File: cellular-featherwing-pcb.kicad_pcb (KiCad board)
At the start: 2 copper layers, 27 x 54 mm, 80 parts, among them J1 SIM8060-6-0-14-00-A, J2 TSM-116-01-L-SV, J3 TSM-112-01-L-SV, J4 U.FL-R-SMT, J5 U.FL-R-SMT, J5 U.FL-R-SMT(10), U1 BG96, U2 TPS63020QDSJTQ1, U3 TXB0108DQSR, U4 MAX8868EUK30+T

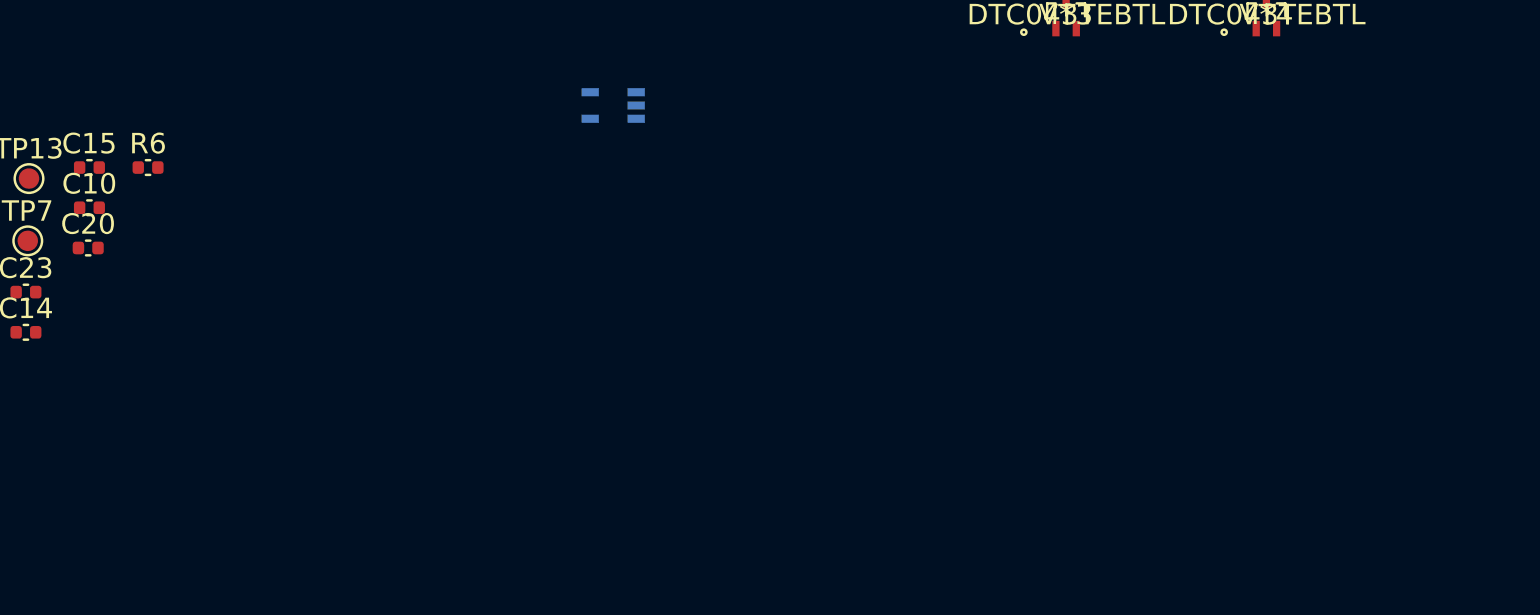
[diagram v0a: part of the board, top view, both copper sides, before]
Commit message: Fixed drc and imported to pcb
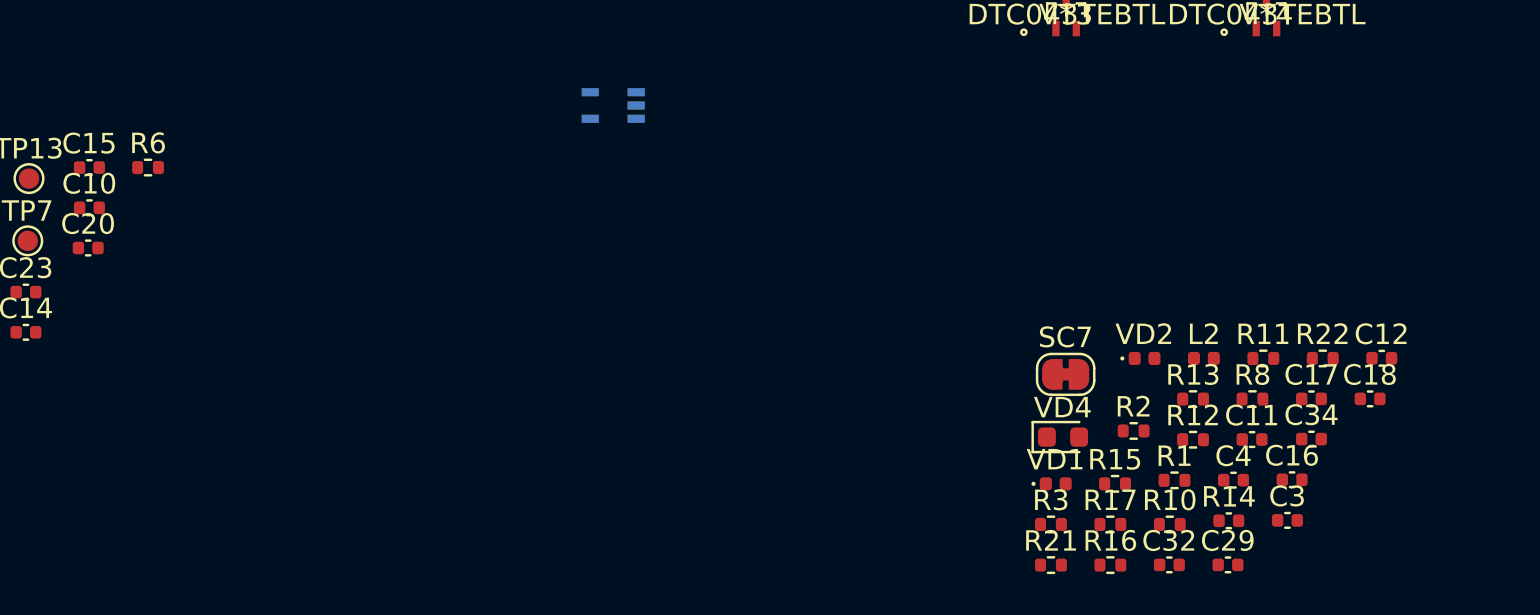
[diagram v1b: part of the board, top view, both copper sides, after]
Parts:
- added C11: 0.1, Capacitor_SMD:C_0402_1005Metric, F.Cu at (155.8, 153.5)
- added C12: 100pF, Capacitor_SMD:C_0402_1005Metric, F.Cu at (162.1, 149.5)
- added C16: 33pF, Capacitor_SMD:C_0402_1005Metric, F.Cu at (157.7, 155.5)
- added C17: 33pF, Capacitor_SMD:C_0402_1005Metric, F.Cu at (158.7, 151.5)
- added C18: 33pF, Capacitor_SMD:C_0402_1005Metric, F.Cu at (161.5, 151.5)
- added C29: 0.1, Capacitor_SMD:C_0402_1005Metric, F.Cu at (154.6, 159.7)
- added C3: 2.2uF, Capacitor_SMD:C_0402_1005Metric, F.Cu at (157.5, 157.5)
- added C32: 0.1, Capacitor_SMD:C_0402_1005Metric, F.Cu at (151.7, 159.7)
- added C34: 0.1, Capacitor_SMD:C_0402_1005Metric, F.Cu at (158.7, 153.5)
- added C4: 0.1uF, Capacitor_SMD:C_0402_1005Metric, F.Cu at (154.8, 155.5)
- added L2: 47nH, Inductor_SMD:L_0402_1005Metric, F.Cu at (153.4, 149.6)
- added R1: 1.24M, Resistor_SMD:R_0402_1005Metric, F.Cu at (151.9, 155.5)
- added R10: 10k, Resistor_SMD:R_0402_1005Metric, F.Cu at (151.7, 157.7)
- added R11: 1k, Resistor_SMD:R_0402_1005Metric, F.Cu at (156.3, 149.6)
- added R12: 1k, Resistor_SMD:R_0402_1005Metric, F.Cu at (152.9, 153.5)
- added R13: 1k, Resistor_SMD:R_0402_1005Metric, F.Cu at (152.9, 151.5)
- added R14: 470, Capacitor_SMD:C_0402_1005Metric, F.Cu at (154.6, 157.5)
- added R15: 100k, Resistor_SMD:R_0402_1005Metric, F.Cu at (149.0, 155.7)
- added R16: 10k, Resistor_SMD:R_0402_1005Metric, F.Cu at (148.8, 159.7)
- added R17: 10k, Resistor_SMD:R_0402_1005Metric, F.Cu at (148.8, 157.7)
- added R2: 182k, Resistor_SMD:R_0402_1005Metric, F.Cu at (149.9, 153.1)
- added R21: 0, Resistor_SMD:R_0402_1005Metric, F.Cu at (145.9, 159.7)
- added R22: 0, Resistor_SMD:R_0402_1005Metric, F.Cu at (159.2, 149.6)
- added R3: 0, Resistor_SMD:R_0402_1005Metric, F.Cu at (145.9, 157.7)
- added R8: 15k, Resistor_SMD:R_0402_1005Metric, F.Cu at (155.8, 151.5)
- added SC7: SolderJumper_2_Bridged, Jumper:SolderJumper-2_P1.3mm_Bridged_RoundedPad1.0x1.5mm, F.Cu at (146.6, 150.3)
- added VD1: D_TVS, Diode_SMD:D_0402_1005Metric, F.Cu at (146.1, 155.7)
- added VD2: D_TVS, Diode_SMD:D_0402_1005Metric, F.Cu at (150.5, 149.6)
- added VD4: BLUE, LED_SMD:LED_0603_1608Metric, F.Cu at (146.5, 153.4)
- R6: footprint Capacitor_SMD:C_0402_1005Metric -> Resistor_SMD:R_0402_1005Metric
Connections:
- D1 pad 1: unconnected-(D1-Pad1) -> Net-(J1-PadC7)

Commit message: starting component layout
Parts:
- moved SC7 165.2 mm to (25.4, 38.1)
- moved C18 118.9 mm to (264.2, 91.4)
- moved C16 118.1 mm to (259.1, 94.8)
- moved C17 117.0 mm to (259.1, 91.4)
- moved SO18 114.3 mm to (17.8, 53.3)
- moved C11 112.9 mm to (261.6, 114.3)
- moved SO13 111.7 mm to (25.1, 33.0)
- moved SO14 105.6 mm to (30.5, 33.0)
- moved SO17 104.8 mm to (25.4, 58.4)
- moved R8 103.6 mm to (251.5, 111.8)
- moved R3 102.8 mm to (233.7, 104.1)
- moved R21 102.2 mm to (236.2, 111.8)
- moved J1 100.1 mm to (246.4, 99.1)
- moved D1 99.6 mm to (259.1, 104.1)
- moved SO15 99.1 mm to (30.5, 38.1)
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
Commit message: Placement work
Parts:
- moved locked 111.0 mm to (146.3, 104.7), turned to 180 degrees
- moved J4 47.4 mm to (218.2, 136.9)
- moved J5 47.4 mm to (213.0, 136.9)
- moved U1 43.7 mm to (163.7, 42.4)
- moved J3 36.9 mm to (151.4, 84.3), turned to 180 degrees
- moved C11 33.2 mm to (252.1, 82.5), turned to -90 degrees
- moved U4 32.5 mm to (97.1, 68.2)
- moved U3 31.1 mm to (199.1, 54.7)
- moved R21 29.6 mm to (253.1, 87.5), turned to 90 degrees
- moved J1 25.5 mm to (248.9, 73.7), turned to 180 degrees
- moved R22 24.1 mm to (249.5, 87.9), turned to 90 degrees
- moved D1 23.5 mm to (248.9, 83.0)
- moved FB1 23.1 mm to (106.7, 93.7)
- moved R3 22.5 mm to (246.6, 85.7), turned to 90 degrees
- moved C18 19.5 mm to (246.6, 83.0), turned to -90 degrees
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- renumbered J2 to locked
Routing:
- net Net-(J1-PadC3): track 0.00 -> 7.22 mm
- net Net-(J1-PadC2): track 0.00 -> 2.84 mm
- net Net-(J1-PadC7): track 0.00 -> 2.12 mm
- net SIM_VDD: track 0.00 -> 1.56 mm
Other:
- board size 27 x 54 mm -> 54 x 27 mm

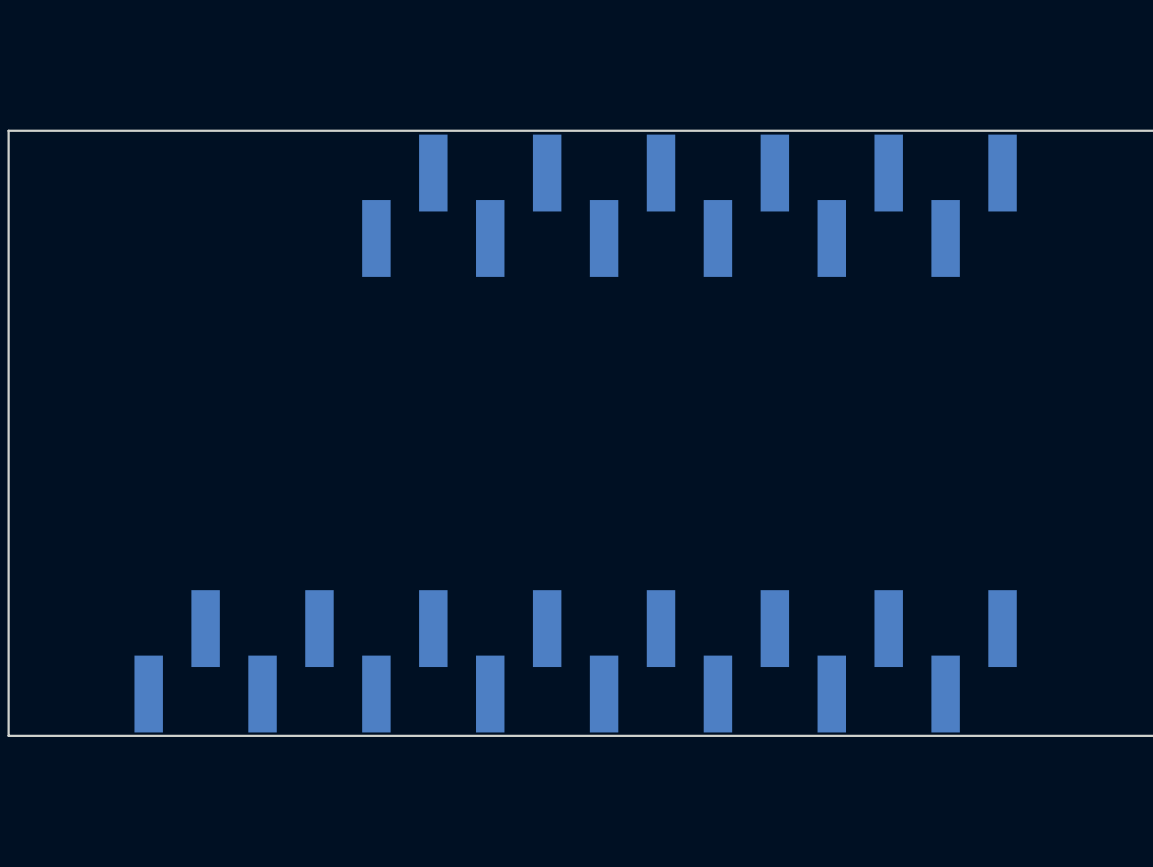
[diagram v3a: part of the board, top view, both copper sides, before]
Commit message: Finished board outline and feather placements
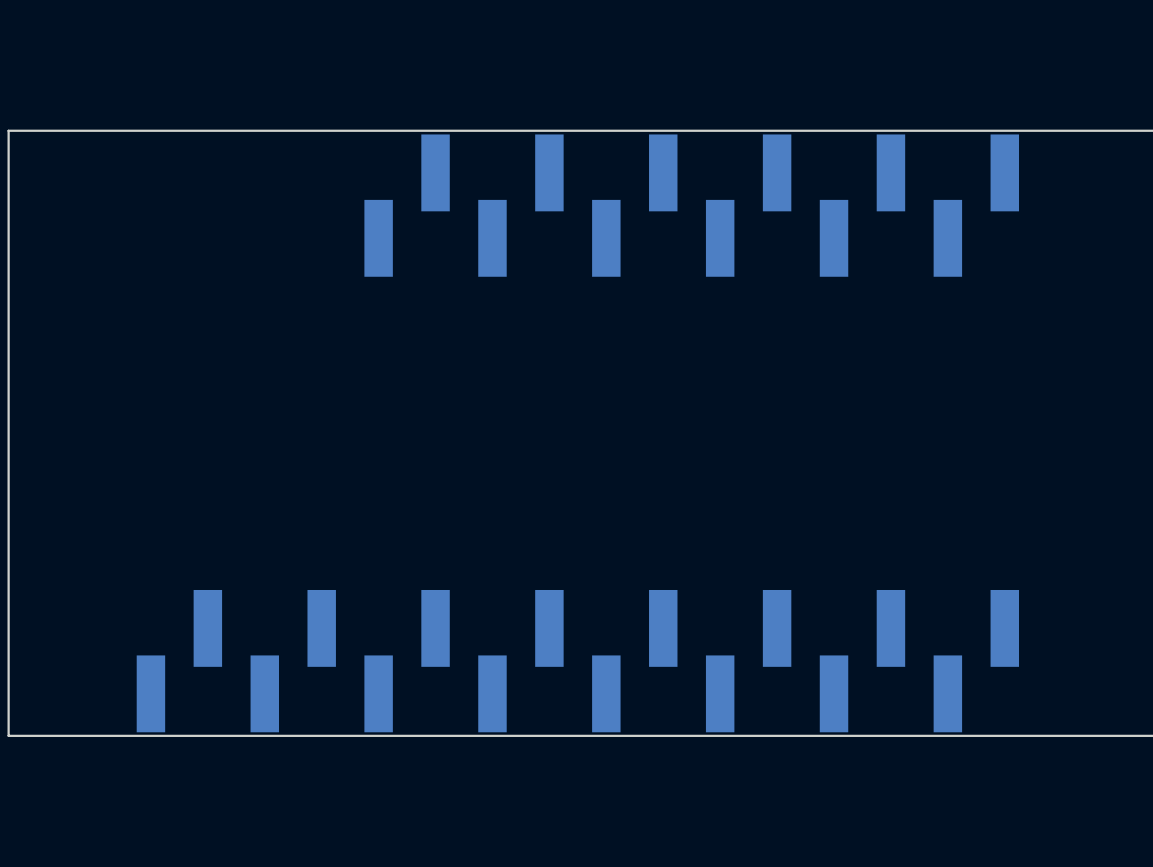
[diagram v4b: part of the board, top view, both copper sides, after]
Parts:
- moved J2 0.10 mm to (146.4, 104.7)
- moved J3 0.10 mm to (151.5, 84.3)
- renumbered locked to J2
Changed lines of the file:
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@@
       (net 24 "GSM_DTR") (pinfunction "1") (pintype "passive"))
   )
-  (footprint "TSM-116-01-L-SV:SAMTEC_TSM-116-01-L-SV" (layer "B.Cu")
-    (at 146.3 104.67375 180)
+  (footprint "TSM-116-01-L-SV:SAMTEC_TSM-116-01-L-SV" locked (layer "B.Cu")
+    (at 146.4 104.666 180)
     (property "MANUFACTURER" "SAMTEC")
     (property "MPN" "TSM-116-01-L-SV")
@@
     (property "Sheetname" "")
     (attr through_hole)
-    (fp_text reference locked "J2" (at -17.145 4.825) (layer "B.SilkS")
+    (fp_text reference "J2" (at 21.4 0) (layer "B.SilkS")
       (effects (font (size 1 1) (thickness 0.15)) (justify mirror))
     )
@@
     (fp_line (start -20.32 -1.27) (end -17.78 -1.27) (layer "B.SilkS") (width 0.2))
     (fp_line (start 17.78 1.27) (end 20.32 1.27) (layer "B.SilkS") (width 0.2))
-    (fp_circle (center 19.3 -3.935) (end 19.4 -3.935) (layer "B.SilkS") (width 0.2) (fill none))
+    (fp_circle (center 20.3 -2.1) (end 20.4 -2.1) (layer "B.SilkS") (width 0.2) (fill none))
     (fp_line (start -20.57 3.425) (end 20.57 3.425) (layer "B.CrtYd") (width 0.05))
     (fp_line (start -20.57 -3.425) (end -20.57 3.425) (layer "B.CrtYd") (width 0.05))
@@
     (fp_line (start 20.32 -1.27) (end -20.32 -1.27) (layer "B.Fab") (width 0.1))
     (fp_line (start -20.32 1.27) (end 20.32 1.27) (layer "B.Fab") (width 0.1))
-    (fp_circle (center 19.3 -3.935) (end 19.4 -3.935) (layer "B.Fab") (width 0.2) (fill none))
+    (fp_circle (center 20.3 -2.1) (end 20.4 -2.1) (layer "B.Fab") (width 0.2) (fill none))
     (pad "01" smd rect locked (at 19.05 -1.46 180) (size 1.27 3.43) (layers "B.Cu" "B.Paste" "B.Mask")
       (net 31 "unconnected-(J2-Pad01)") (pinfunction "01") (pintype "passive"))
@@
     (pad "16" smd rect locked (at -19.05 1.46 180) (size 1.27 3.43) (layers "B.Cu" "B.Paste" "B.Mask")
       (net 39 "unconnected-(J2-Pad16)") (pinfunction "16") (pintype "passive"))
+    (model "${KIPRJMOD}/snapeda/TSM-116-01-L-SV/TSM-116-01-L-SV.step"
+      (offset (xyz 0 0 1.3))
+      (scale (xyz 1 1 1))
+      (rotate (xyz -90 0 0))
+    )
   )
   (footprint "SN74AHC1G09DCKR:SN74AHC1G09DCKR" (layer "B.Cu")
@@
       (net 98 "Net-(U4-Pad5)") (pinfunction "BP") (pintype "output"))
   )
-  (footprint "TSM-112-01-L-SV:SAMTEC_TSM-112-01-L-SV" (layer "B.Cu")
-    (at 151.38 84.34625 180)
+  (footprint "TSM-112-01-L-SV:SAMTEC_TSM-112-01-L-SV" locked (layer "B.Cu")
+    (at 151.48 84.34 180)
     (property "MANUFACTURER" "SAMTEC")
     (property "MPN" "TSM-112-01-L-SV")
@@
     (property "Sheetname" "")
     (attr through_hole)
-    (fp_text reference "J3" (at -12.065 4.825) (layer "B.SilkS")
+    (fp_text reference "J3" (at 16.48 0) (layer "B.SilkS")
       (effects (font (size 1 1) (thickness 0.15)) (justify mirror))
     )
@@
     (fp_line (start 15.24 1.27) (end 15.24 -1.27) (layer "B.SilkS") (width 0.2))
     (fp_line (start 12.7 1.27) (end 15.24 1.27) (layer "B.SilkS") (width 0.2))
-    (fp_circle (center 14.22 -3.935) (end 14.32 -3.935) (layer "B.SilkS") (width 0.2) (fill none))
+    (fp_circle (center 15.2 -2.2) (end 15.3 -2.2) (layer "B.SilkS") (width 0.2) (fill none))
     (fp_line (start 15.49 3.425) (end 15.49 -3.425) (layer "B.CrtYd") (width 0.05))
     (fp_line (start -15.49 3.425) (end 15.49 3.425) (layer "B.CrtYd") (width 0.05))
@@
     (fp_line (start 15.24 1.27) (end 15.24 -1.27) (layer "B.Fab") (width 0.1))
     (fp_line (start -15.24 1.27) (end 15.24 1.27) (layer "B.Fab") (width 0.1))
-    (fp_circle (center 14.22 -3.935) (end 14.32 -3.935) (layer "B.Fab") (width 0.2) (fill none))
+    (fp_circle (center 15.2 -2.2) (end 15.3 -2.2) (layer "B.Fab") (width 0.2) (fill none))
     (pad "01" smd rect locked (at 13.97 -1.46 180) (size 1.27 3.43) (layers "B.Cu" "B.Paste" "B.Mask")
       (net 51 "VBAT") (pinfunction "01") (pintype "passive"))
@@
     (pad "12" smd rect locked (at -13.97 1.46 180) (size 1.27 3.43) (layers "B.Cu" "B.Paste" "B.Mask")
       (net 60 "I2C_SDA") (pinfunction "12") (pintype "passive"))
+    (model "${KIPRJMOD}/snapeda/TSM-112-01-L-SV/TSM-112-01-L-SV.step"
+      (offset (xyz 0 0 1.3))
+      (scale (xyz 1 1 1))
+      (rotate (xyz -90 0 0))
+    )
   )
   (gr_rect locked (start 121 108) (end 175 81) (layer "Edge.Cuts") (width 0.1) (fill none))
@@
   (segment (start 245.6 80.605) (end 245.745 80.46) (width 0.25) (layer "F.Cu") (net 91))
   (segment (start 245.6 82.52) (end 245.6 80.605) (width 0.25) (layer "F.Cu") (net 91))
-  (group "" (id cb48c930-a83c-4b16-9674-8f301bb21e12)
+  (group "" locked (id e56ddc77-ec70-45ce-be4e-8d98e122b0c5)
     (members
       191bc690-4ba3-4d26-9edd-91f93ca6e16e
       c5fb625d-d5c8-460a-95e8-b489f7626af4
+      f15b49d4-2b36-48bf-8810-ca7c1860c448
     )
   )

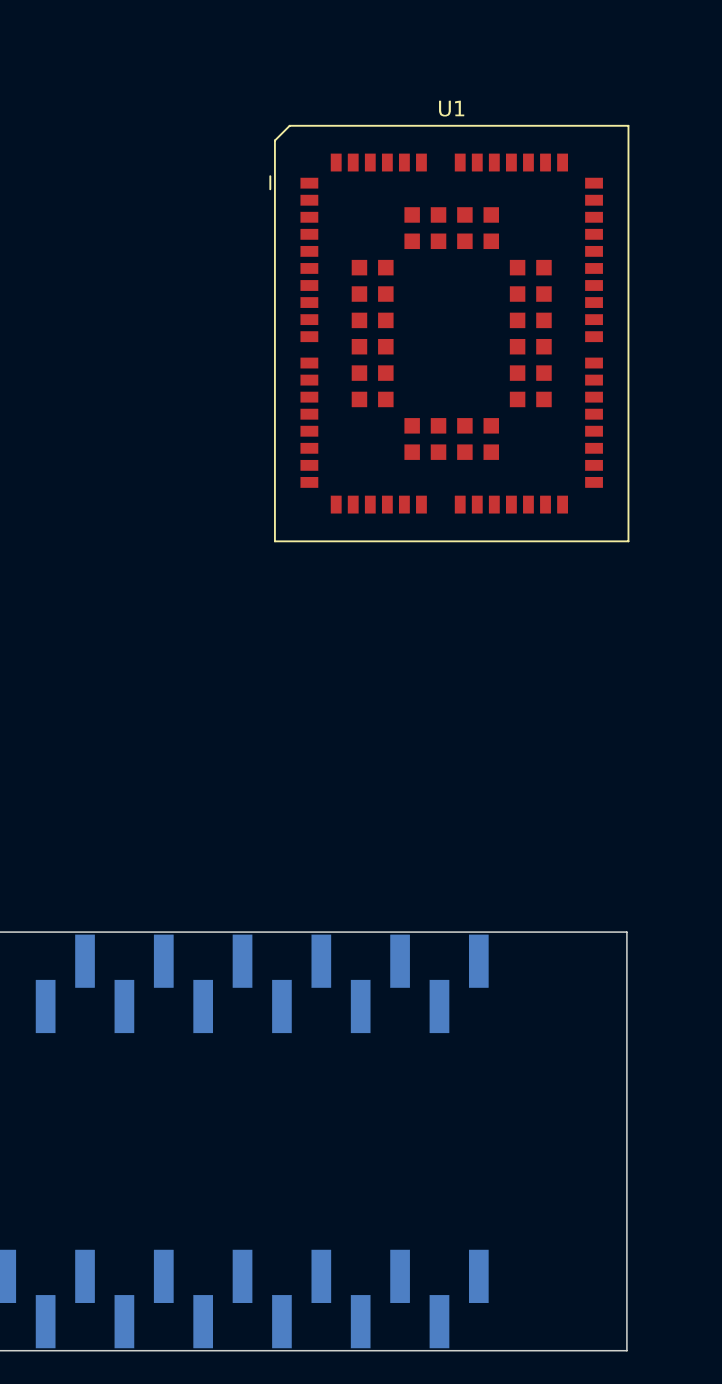
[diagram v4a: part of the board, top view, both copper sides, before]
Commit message: Placed quectel
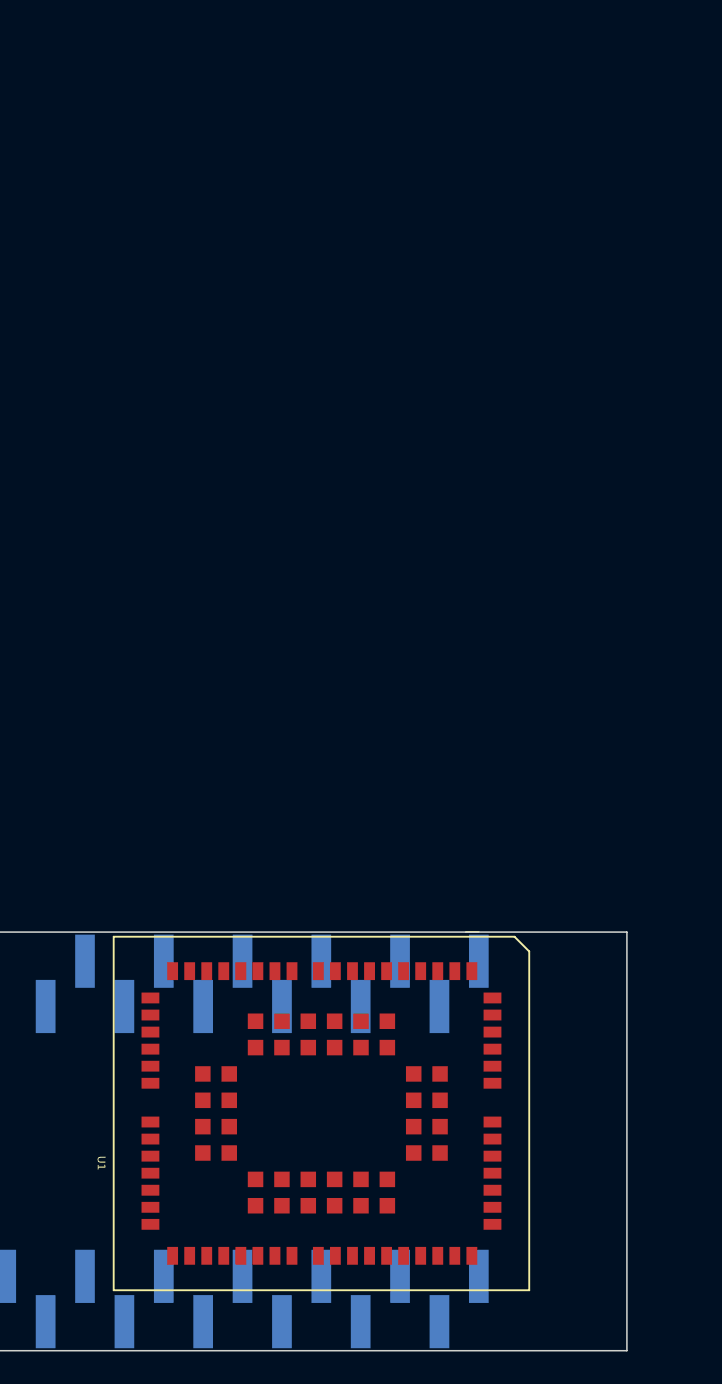
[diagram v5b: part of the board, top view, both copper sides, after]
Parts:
- moved U1 51.0 mm to (155.3, 92.7), turned to -90 degrees

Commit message: Parts placement
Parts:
- removed the J5 at (213.0, 136.9)
- moved R7 139.2 mm to (184.2, 110.0)
- moved R8 126.2 mm to (127.8, 105.2)
- moved C13 123.2 mm to (190.7, 85.7)
- moved C9 121.3 mm to (184.8, 85.7)
- moved J1 118.9 mm to (131.2, 90.4)
- moved C11 118.9 mm to (134.4, 99.2)
- moved C16 118.9 mm to (127.9, 99.7)
- moved C17 118.9 mm to (133.1, 99.2)
- moved C18 118.9 mm to (128.9, 99.7)
- moved D1 118.9 mm to (131.2, 99.7)
- moved R21 118.9 mm to (135.4, 104.2)
- moved R22 118.9 mm to (131.8, 104.6)
- moved R3 118.9 mm to (128.9, 102.4)
- moved C22 115.9 mm to (169.5, 98.8), turned to -90 degrees
- moved C25 113.8 mm to (149.3, 105.5), turned to -90 degrees
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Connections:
- C21 pad 1: VBAT_RF -> VBAT_BB
- C23 pad 1: VBAT_RF -> VBAT_BB
- C25 pad 1: VBAT_RF -> VBAT_BB
- C28 pad 1: VBAT_RF -> VBAT_BB
- FB4 pad 1: VBAT_RF -> VBAT_BB
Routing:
- net VBAT_BB: track 0.00 -> 5.20 mm
- added copper zone on B.Cu, net GND
- added copper zone on F.Cu, net GND
